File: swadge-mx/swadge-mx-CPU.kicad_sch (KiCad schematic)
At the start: 5 parts, among them U3 ESP32-S3-WROOM-1

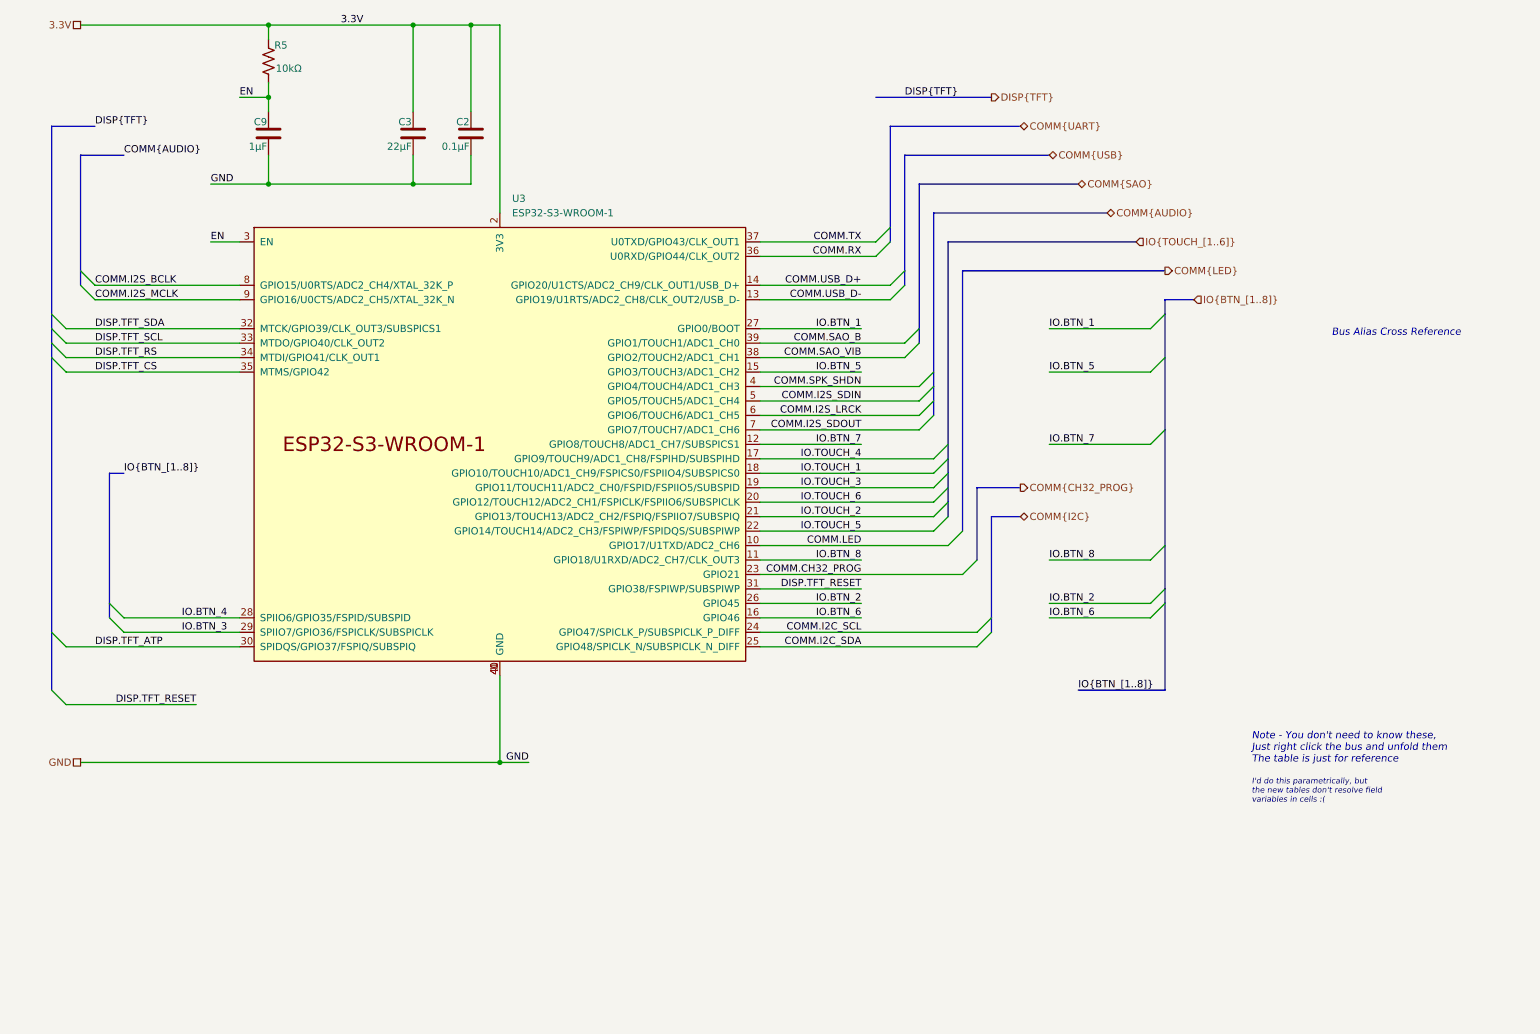
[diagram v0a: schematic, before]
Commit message: Further Subdivide Sheets
Moved all audio into one sheet, and sub-divided into DAC and amp sheets. Moved all power into one sheet and sub-divided into BMS and Buck.
Cleaned up front page a bit.
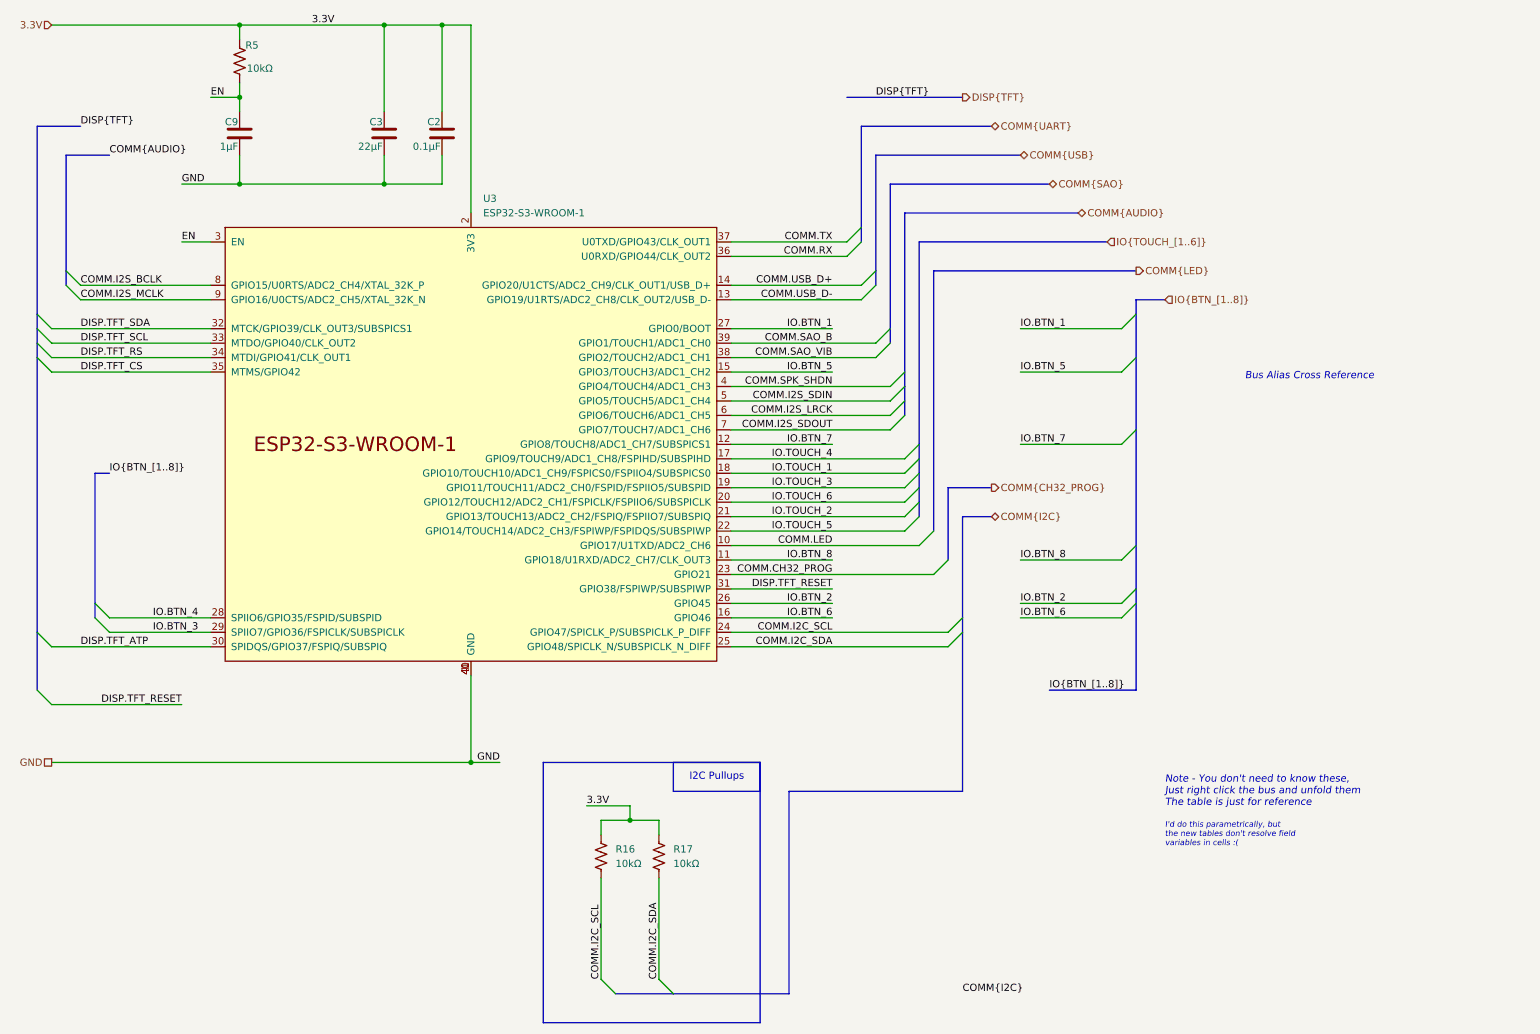
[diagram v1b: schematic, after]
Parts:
- added R16, R17: 10kΩ, Swadge_Parts:R_0603_1608Metric, symbol Swadge_Parts:R_US
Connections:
- net 3.3V: now also R16.1, R17.1
- net COMM.I2C_SCL: now also R16.2
- net COMM.I2C_SDA: now also R17.2
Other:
- note added: "I2C Pullups"
- moved on the sheet: C2, C3, C9, R5, U3
